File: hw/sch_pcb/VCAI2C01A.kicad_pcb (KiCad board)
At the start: 2 copper layers, 60.5 x 40.1 mm, 74 parts, among them J10 JUMP2_2x1, J11 JUMP2_2x1, J13 JUMP_5X2, J14 JUMP_2x1, J15 JUMP_2x1, J16 JUMP_2x1, J17 JUMP_2x1, J18 JUMP_2x1, J19 JUMP_2x1, J2 CONN_2, J20 JUMP_2x1, J21 JUMP_2x1, J22 JUMP_2x1, J23 JUMP_2x1, J3 JUMP_2x1, J4 CONN_2, J5 JUMP_2x1, J6 CONN_2, J7 JUMP_2x1, J8 CONN_2, J9 JUMP_2x1, M1 HOLE, M2 HOLE, M3 HOLE, M4 HOLE, U1 TLC27L2ID, U2 TLC27L2ID, U3 MCP3424

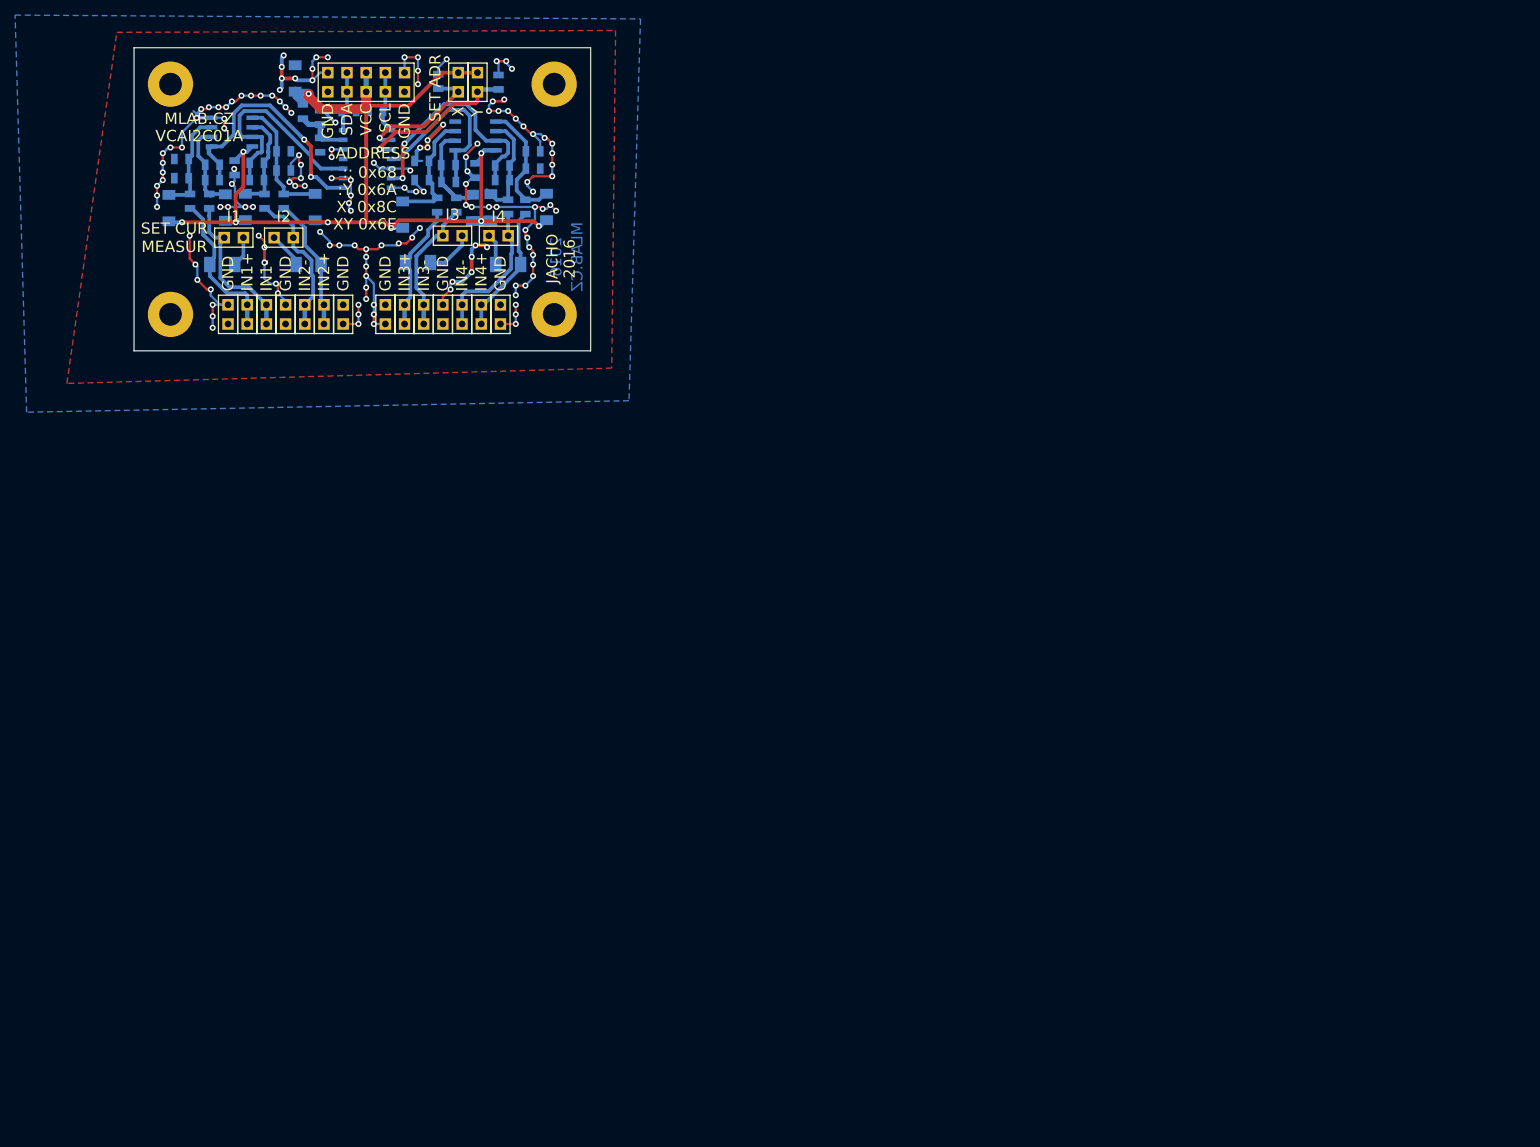
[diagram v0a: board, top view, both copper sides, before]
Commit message: Update to kicad 6.0 Activate github workflow.
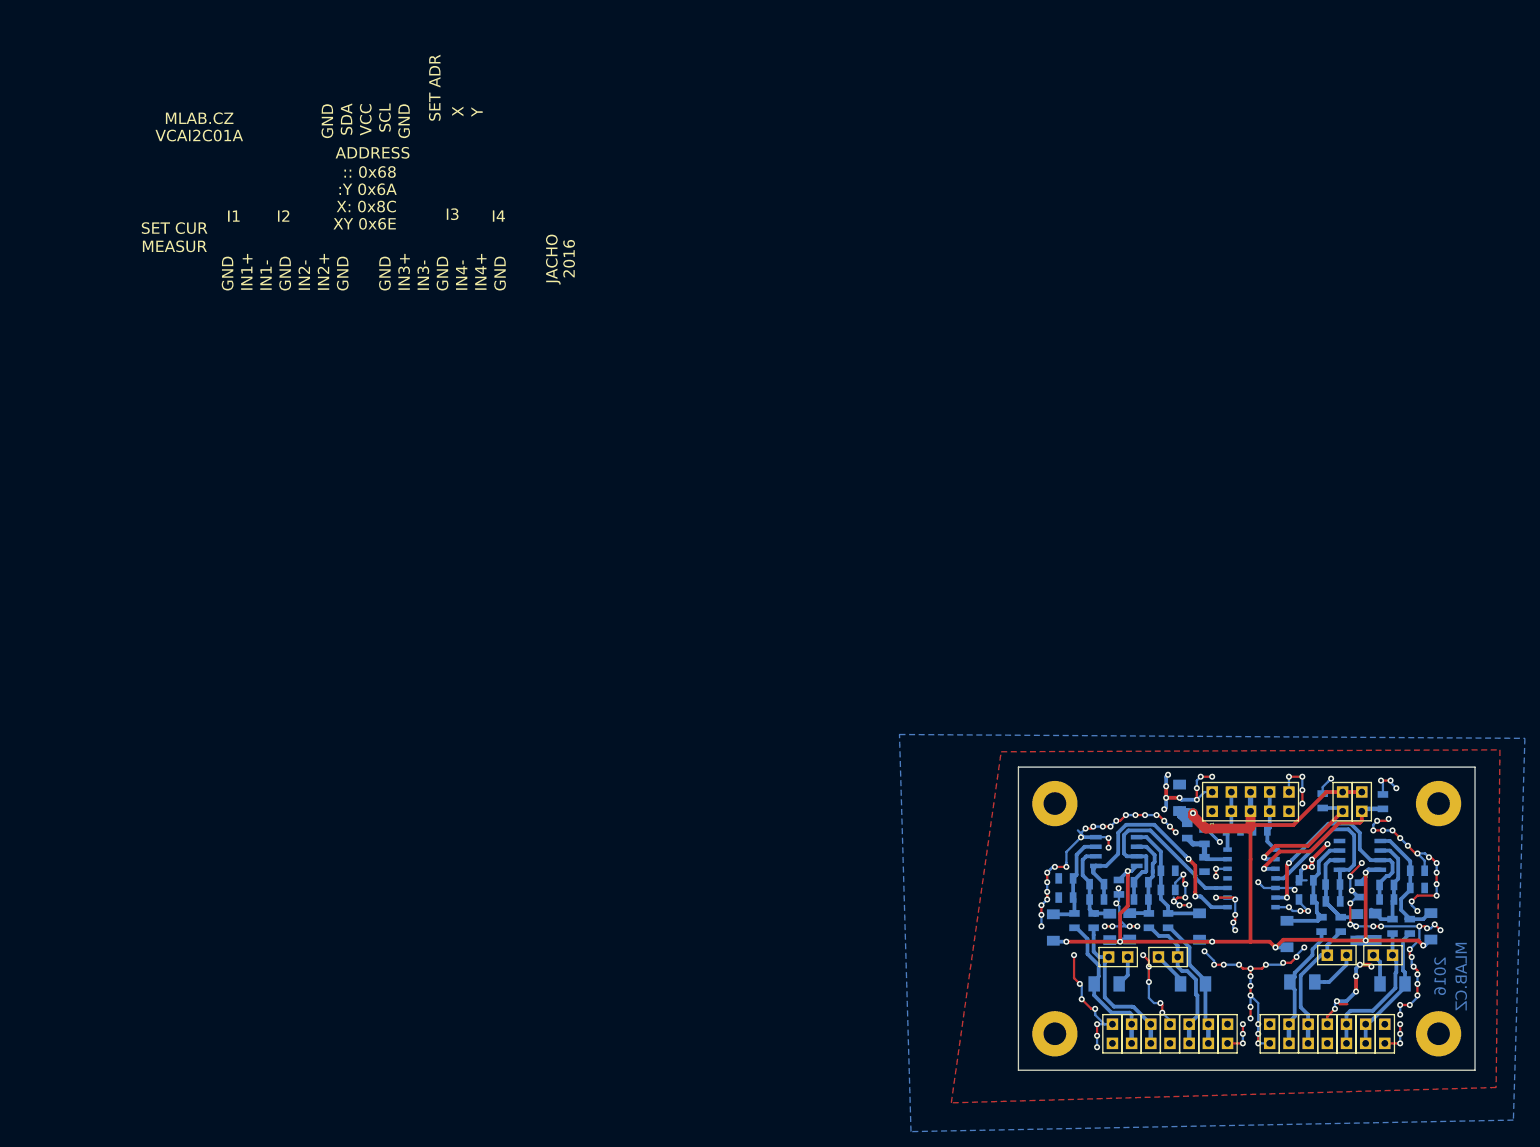
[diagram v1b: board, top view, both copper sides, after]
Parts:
- moved C1 150.9 mm to (123.6, 69.6)
- moved C5 150.9 mm to (130.7, 70.8)
- moved C7 150.9 mm to (133.6, 72.4)
- moved C8 150.9 mm to (155.4, 72.4)
- moved C9 150.9 mm to (170.2, 70.9)
- moved D3 150.9 mm to (132.1, 75.9)
- moved D5 150.9 mm to (141.3, 76.0)
- moved D6 150.9 mm to (162.2, 76.1)
- moved J15 150.9 mm to (140.0, 90.2)
- moved J19 150.9 mm to (153.2, 90.2)
- moved J2 150.9 mm to (130.6, 80.0)
- moved J21 150.9 mm to (160.8, 90.2)
- moved J5 150.9 mm to (129.8, 90.2)
- moved J9 150.9 mm to (132.3, 90.2)
- moved M2 150.9 mm to (122.2, 90.2)
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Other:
- net class Default removed

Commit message: Cleanup copper pour layout. Add powerflags to schematics.
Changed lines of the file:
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@@
   (setup
     (pad_to_mask_clearance 0.2)
-    (aux_axis_origin 111.76 101.6)
+    (aux_axis_origin 122.174 90.17)
     (pcbplotparams
       (layerselection 0x00010e0_ffffffff)
@@
     (effects (font (size 1.5 1.5) (thickness 0.3)))
   )
-  (target plus (at 111.76 101.6) (size 5) (width 0.15) (layer "Edge.Cuts"))
   (segment (start 167.894 90.17) (end 167.894 88.9) (width 0.3) (layer "F.Cu") (net 1))
   (segment (start 122.174 68.072) (end 123.698002 68.072) (width 0.3) (layer "F.Cu") (net 1))
@@
     (polygon
       (pts
-        (xy 115.062 52.832)
-        (xy 181.102 52.578)
-        (xy 180.594 97.282)
-        (xy 108.458 99.314)
+        (xy 115.57 53.34)
+        (xy 179.07 53.34)
+        (xy 179.07 96.52)
+        (xy 115.57 96.52)
       )
     )
@@
     (polygon
       (pts
-        (xy 184.404 51.054)
-        (xy 182.88 101.6)
-        (xy 103.124 103.124)
-        (xy 101.6 50.546)
+        (xy 182.88 50.8)
+        (xy 182.88 99.06)
+        (xy 114.3 99.06)
+        (xy 114.3 50.8)
       )
     )
